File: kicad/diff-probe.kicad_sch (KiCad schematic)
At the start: 29 parts, among them IC3 LMH6702, IC4 LMH6702, IC5 LMH6702, J3 HEADER-1X2CARD-EDGE, J4 CON-1X3-TAB-AMP-29173-3-NARROW, X2 SMA--BU-SMA-H

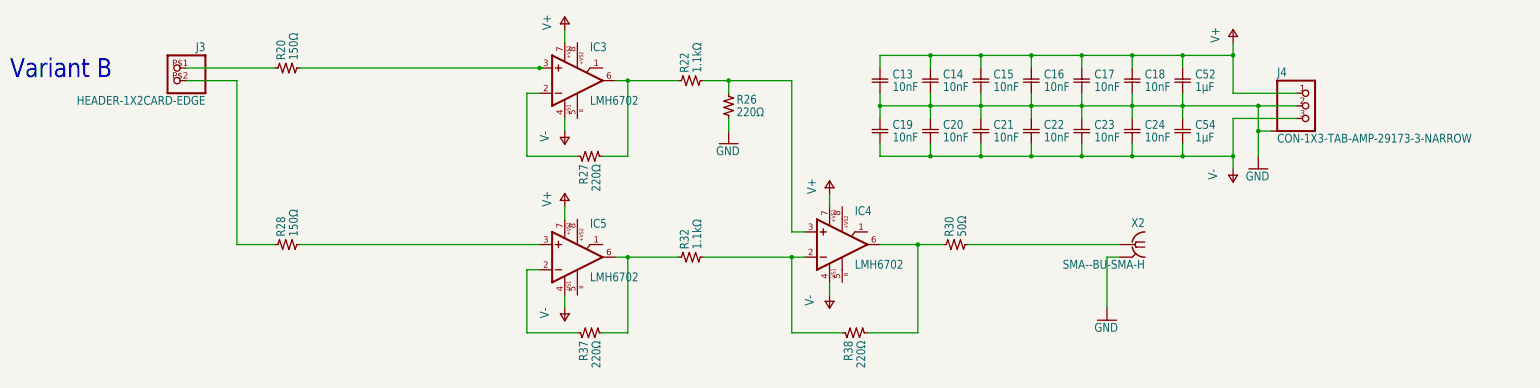
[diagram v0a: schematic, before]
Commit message: give nets names to make the PCB more readable
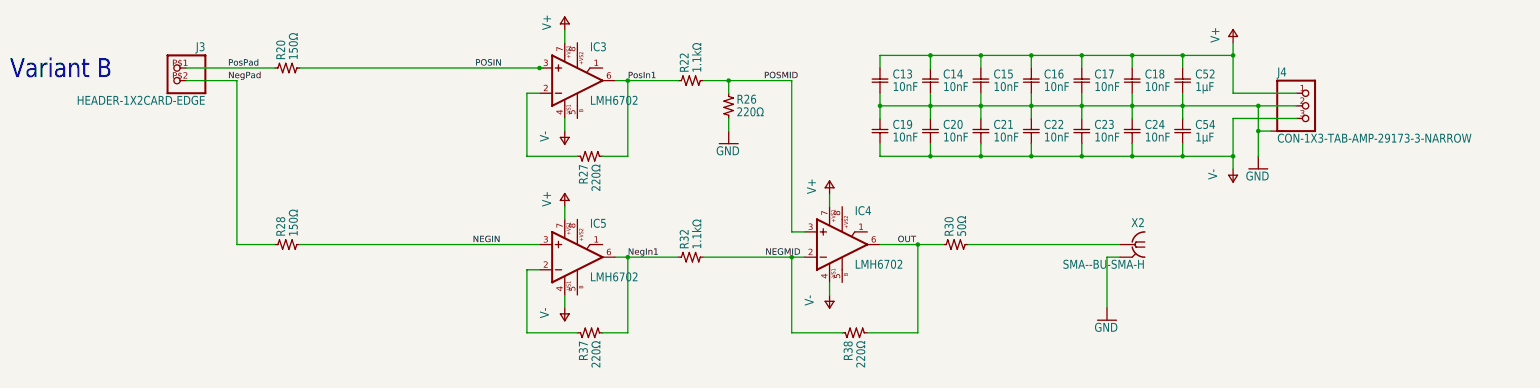
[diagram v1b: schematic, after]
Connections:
- net NegIn1: now reaches IC5.6 (OUT), R32.P$1 (1), R37.P$2 (2)
- net NEGMID: now reaches IC4.2 (-IN), R32.P$2 (2), R38.P$1 (1)
- net PosIn1: now reaches IC3.6 (OUT), R22.P$1 (1), R27.P$2 (2)
- net POSMID: now reaches IC4.3 (+IN), R22.P$2 (2), R26.P$1 (1)
- net OUT: now reaches IC4.6 (OUT), R30.P$1 (1), R38.P$2 (2)
- net NegPad: now reaches J3.P$2 (2), R28.P$1 (1)
- net NEGIN: now reaches IC5.3 (+IN), R28.P$2 (2)
- net PosPad: now reaches J3.P$1 (1), R20.P$1 (1)
- net POSIN: now reaches IC3.3 (+IN), R20.P$2 (2)
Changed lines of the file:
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@@
     (effects (font (size 3.81 3.2385)) (justify left bottom))
+  )
+  (label "POSMID" (at 169.672 71.12 0)
+    (effects (font (size 1.27 1.27)) (justify left bottom))
+  )
+  (label "NEGIN" (at 110.998 104.14 0)
+    (effects (font (size 1.27 1.27)) (justify left bottom))
+  )
+  (label "OUT" (at 196.596 104.14 0)
+    (effects (font (size 1.27 1.27)) (justify left bottom))
+  )
+  (label "PosIn1" (at 142.24 71.12 0)
+    (effects (font (size 1.27 1.27)) (justify left bottom))
+  )
+  (label "NegPad" (at 61.722 71.12 0)
+    (effects (font (size 1.27 1.27)) (justify left bottom))
+  )
+  (label "POSIN" (at 111.506 68.58 0)
+    (effects (font (size 1.27 1.27)) (justify left bottom))
+  )
+  (label "NegIn1" (at 142.24 106.68 0)
+    (effects (font (size 1.27 1.27)) (justify left bottom))
+  )
+  (label "PosPad" (at 61.722 68.58 0)
+    (effects (font (size 1.27 1.27)) (justify left bottom))
+  )
+  (label "NEGMID" (at 169.926 106.68 0)
+    (effects (font (size 1.27 1.27)) (justify left bottom))
   )
   (symbol (lib_id "diff-probe-eagle-import:R-US-0402-SQUARE") (at 154.94 106.68 90) (unit 1)

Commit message: optimize output
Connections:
- net OutPad: now reaches R30.P$2 (2), X2.1
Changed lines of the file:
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@@
+    (effects (font (size 1.27 1.27)) (justify left bottom))
+  )
+  (label "OutPad" (at 216.916 104.14 0)
     (effects (font (size 1.27 1.27)) (justify left bottom))
   )
